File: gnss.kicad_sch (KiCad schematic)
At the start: 72 parts, among them J11 SMA-KE-347-H13.5-1.6, J12 U.FL, Q12 AO3401A, Q13 BSS138, SW4 RESET_GNSS, SW5 SAFEBOOT_GNSS, U10 TPS7A2033PDBVR, U11 TPS259474LRPWR, U9 NEO-F10N

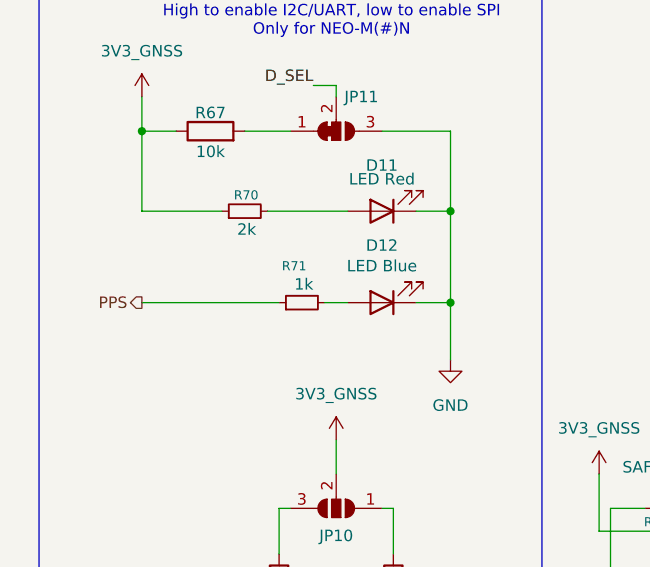
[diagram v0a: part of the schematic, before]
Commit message: schematic: add D24/D25 PZU12B2L zeners, Q_NMOS_SGD symbol, misc sheet edits
Co-Authored-By: Claude Opus 5.5 <noreply@anthropic.com>
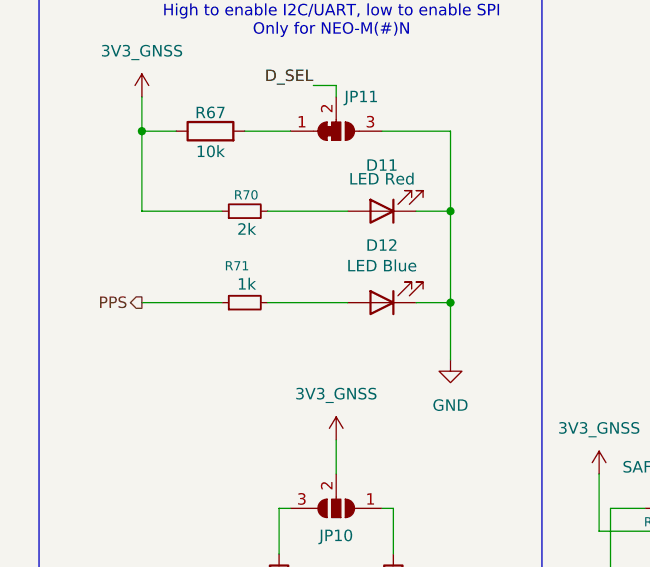
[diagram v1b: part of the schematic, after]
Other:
- moved on the sheet: R71
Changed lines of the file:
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@@
 	(wire
 		(pts
-			(xy 49.53 59.69) (xy 46.99 59.69)
+			(xy 49.53 59.69) (xy 40.64 59.69)
 		)
 		(stroke
@@
 	(wire
 		(pts
-			(xy 26.67 59.69) (xy 41.91 59.69)
+			(xy 26.67 59.69) (xy 35.56 59.69)
 		)
 		(stroke
@@
 	(symbol
 		(lib_id "Device:R_Small")
-		(at 44.45 59.69 90)
+		(at 38.1 59.69 90)
 		(unit 1)
 		(body_style 1)
@@
 		(dnp no)
 		(property "Reference" "R71"
-			(at 44.958 55.626 90)
+			(at 38.608 55.626 90)
 			(show_name no)
 			(do_not_autoplace no)
@@
 		)
 		(property "Value" "1k"
-			(at 45.72 57.658 90)
+			(at 39.37 57.658 90)
 			(show_name no)
 			(do_not_autoplace no)
@@
 		)
 		(property "Footprint" "Resistor_SMD:R_0402_1005Metric"
-			(at 44.45 59.69 0)
+			(at 38.1 59.69 0)
 			(hide yes)
 			(show_name no)
@@
 		)
 		(property "Datasheet" "https://datasheet.lcsc.com/datasheet/pdf/dcb62c832dd79d37c154ec20e16fb58d.pdf?productCode=C48533754"
-			(at 44.45 59.69 0)
+			(at 38.1 59.69 0)
 			(hide yes)
 			(show_name no)
@@
 		)
 		(property "Description" "RES 1kΩ ±0.1% 62.5mW 0402 thick film"
-			(at 44.45 59.69 0)
+			(at 38.1 59.69 0)
 			(hide yes)
 			(show_name no)
@@
 		)
 		(property "MPN" "FRH0402B1001TS"
-			(at 44.45 59.69 0)
+			(at 38.1 59.69 0)
 			(hide yes)
 			(show_name no)
@@
 		)
 		(property "Manufacturer" "FOJAN"
-			(at 44.45 59.69 0)
+			(at 38.1 59.69 0)
 			(hide yes)
 			(show_name no)
@@
 		)
 		(property "LCSC Part" "C48533754"
-			(at 44.45 59.69 0)
+			(at 38.1 59.69 0)
 			(hide yes)
 			(show_name no)
@@
 		)
 		(property "Tolerance" "0.1%"
-			(at 44.45 59.69 0)
+			(at 38.1 59.69 0)
 			(hide yes)
 			(show_name no)
@@
 		)
 		(property "Power Rating" "62.5mW"
-			(at 44.45 59.69 0)
+			(at 38.1 59.69 0)
 			(hide yes)
 			(show_name no)

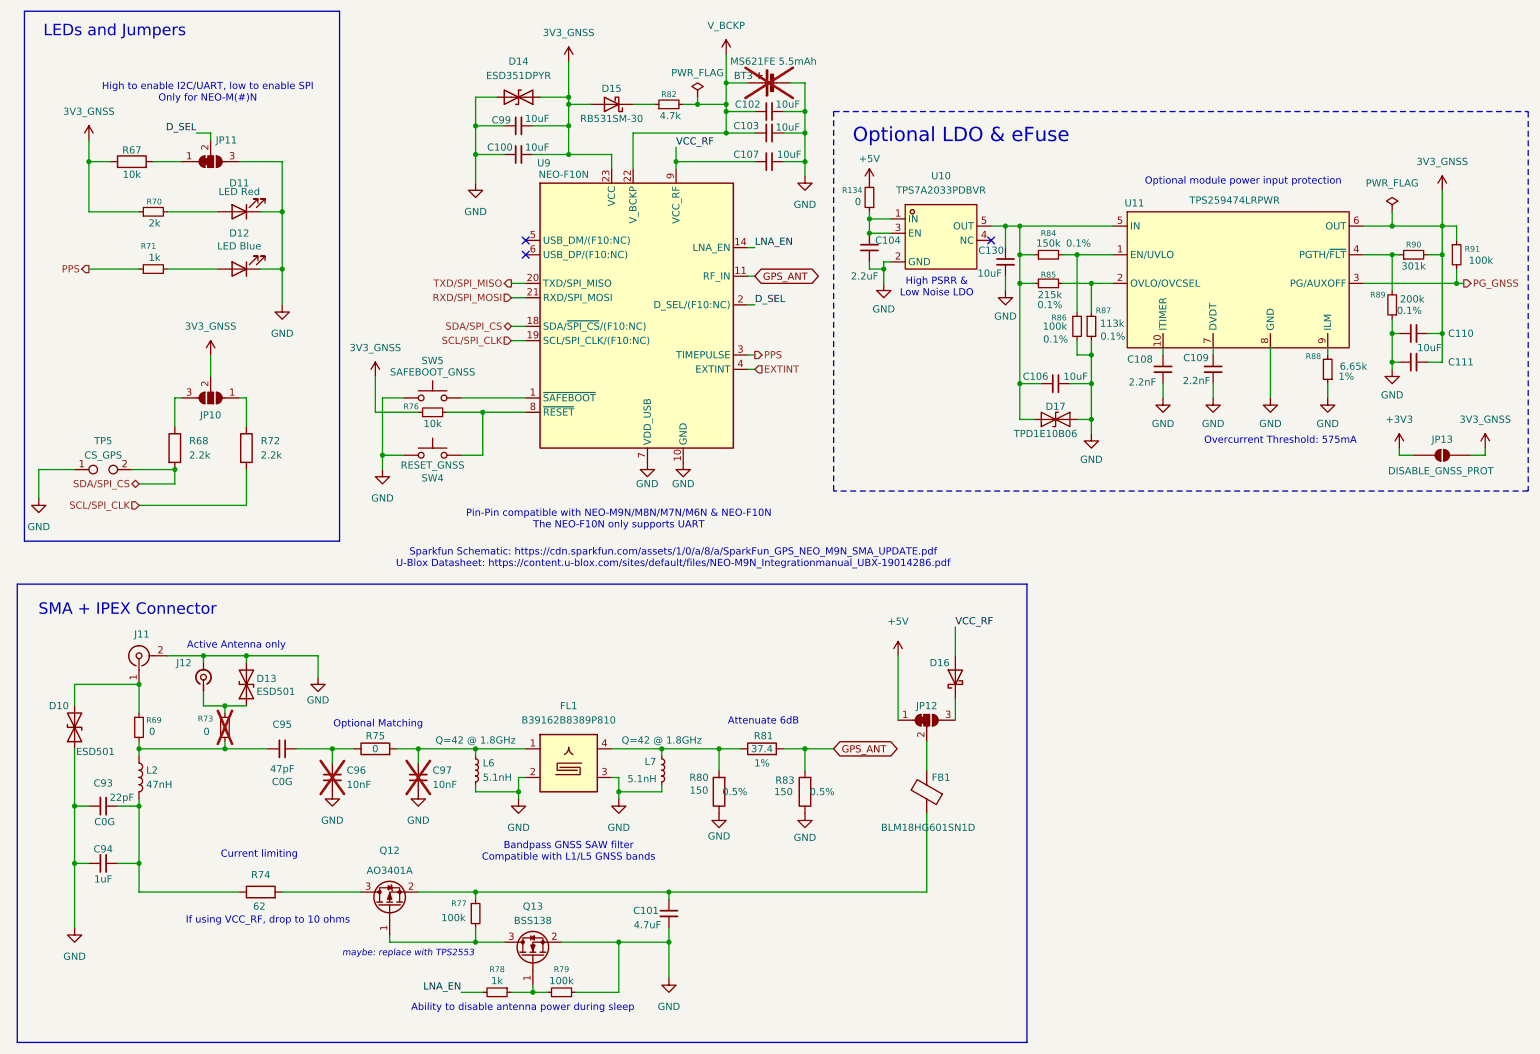
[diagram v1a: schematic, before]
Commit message: checkpoint: schematic WIP before battery -> charger rename
Connectors and Overview sheets, LSM6DSV16X/TPS22945/charger datasheets,
and in-progress edits across all sheets, committed as-is so the rename
diff stands alone.

Co-Authored-By: Claude Opus 5.5 <noreply@anthropic.com>
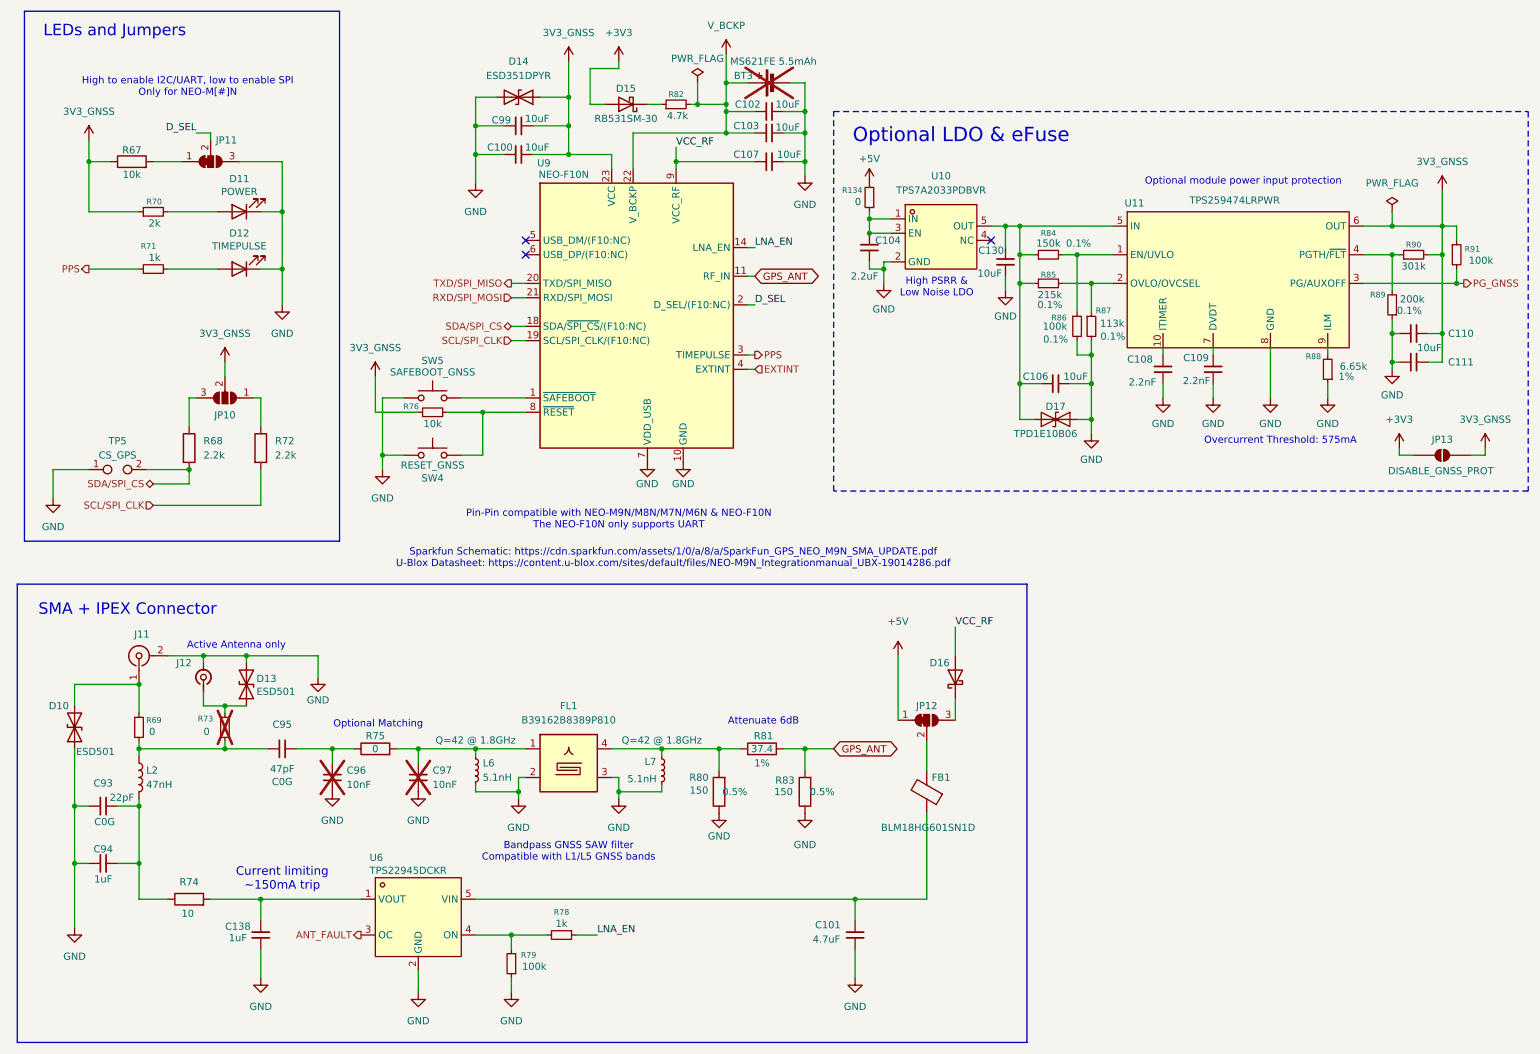
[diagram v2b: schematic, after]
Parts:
- removed Q12: AO3401A, Package_TO_SOT_SMD:SOT-23, symbol Transistor_FET:AO3401A
- removed Q13: BSS138, Package_TO_SOT_SMD:SOT-23, symbol Transistor_FET:BSS138
- removed R77: 100k, Resistor_SMD:R_0402_1005Metric, symbol Device:R_Small
- added C138: 1uF, Capacitor_SMD:C_0402_1005Metric, symbol Device:C_Small
- added U6: TPS22945DCKR, Package_TO_SOT_SMD:SOT-353_SC-70-5, symbol easyeda2kicad:TPS22945DCKR
- D11: value LED Red -> POWER
- D12: value LED Blue -> TIMEPULSE
- R74: value 62 -> 10; footprint Resistor_SMD:R_0805_2012Metric -> Resistor_SMD:R_0603_1608Metric_Pad0.98x0.95mm_HandSolder; LCSC Part C560547 -> (none); MPN AS05W2J0620T5E -> (none); Manufacturer UNI-ROYAL -> (none); Power Rating 500mW -> 250mW; Tolerance 5% -> 1%
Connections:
- net +3V3: now also D15.2 (A)
- net 3V3_GNSS: no longer D15.2 (A)
- net GND: now also R79.1, C138.2, U6.2 (GND); no longer R79.2
- net LNA_EN: now also R78.1; no longer R78.2
- net at C101.1, FB1.1: now also U6.5 (VIN)
- net at R74.2: now also C138.1, U6.1 (VOUT)
- new net: R78.2, R79.2, U6.4 (ON)
- new net ANT_FAULT: U6.3 (OC)
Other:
- note added: "Current limiting ~150mA trip"
- note added: "High to enable I2C/UART, low to enable SPI Only for NEO-M[#]N"
- note removed: "Ability to disable antenna power during sleep"
- note removed: "Current limiting"
- note removed: "High to enable I2C/UART, low to enable SPI Only for NEO-M(#)N"
- note removed: "If using VCC_RF, drop to 10 ohms"
- note removed: "maybe: replace with TPS2553"
- title: GNSS Module / Active RF Antenna -> GNSS (NEO-F10N) & Active Antenna
- moved on the sheet: C101, D15, JP10, R68, R72, R74, R82, TP5
